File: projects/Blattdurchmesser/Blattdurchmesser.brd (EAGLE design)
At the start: 100 x 80 mm, 14 parts, among them K1 TX2_RELAY", U1 ARDUINOR3-DIMENSION

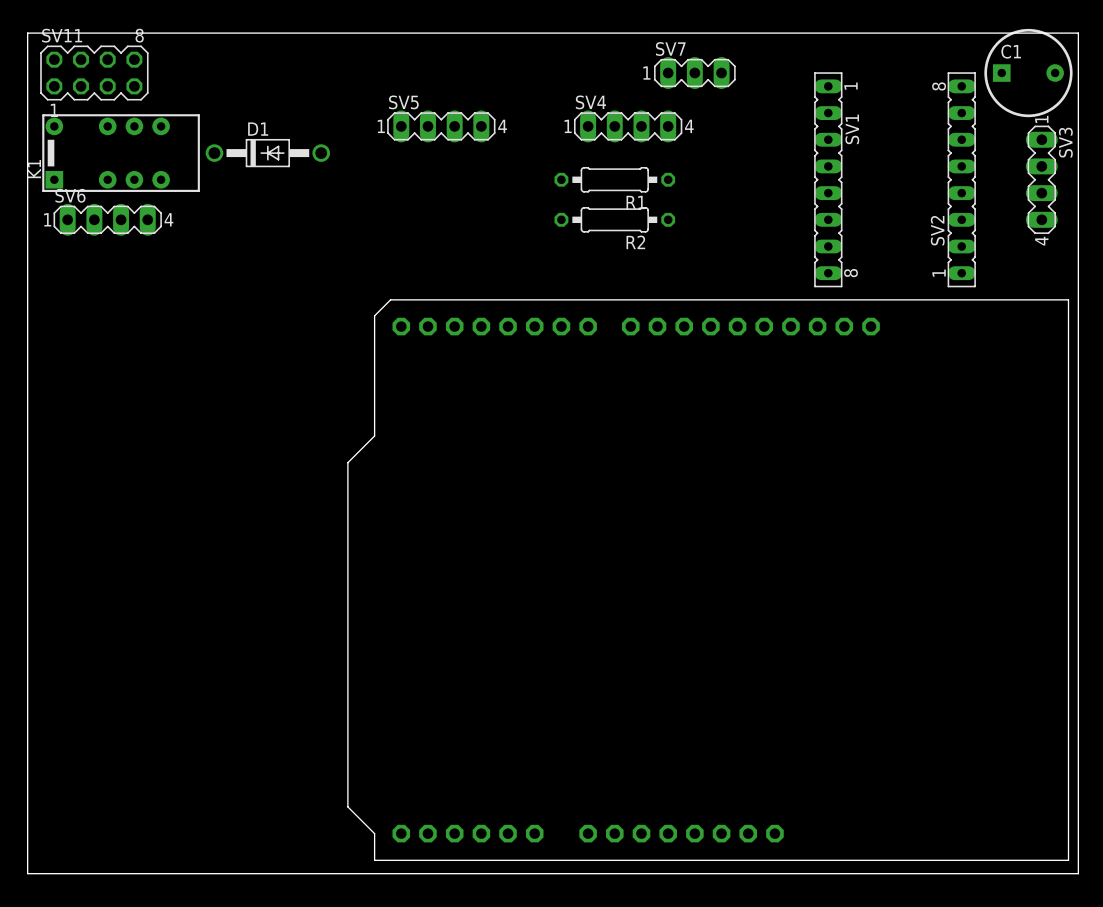
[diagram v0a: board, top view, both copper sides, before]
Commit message: improvement; * parts on pcb rearranged
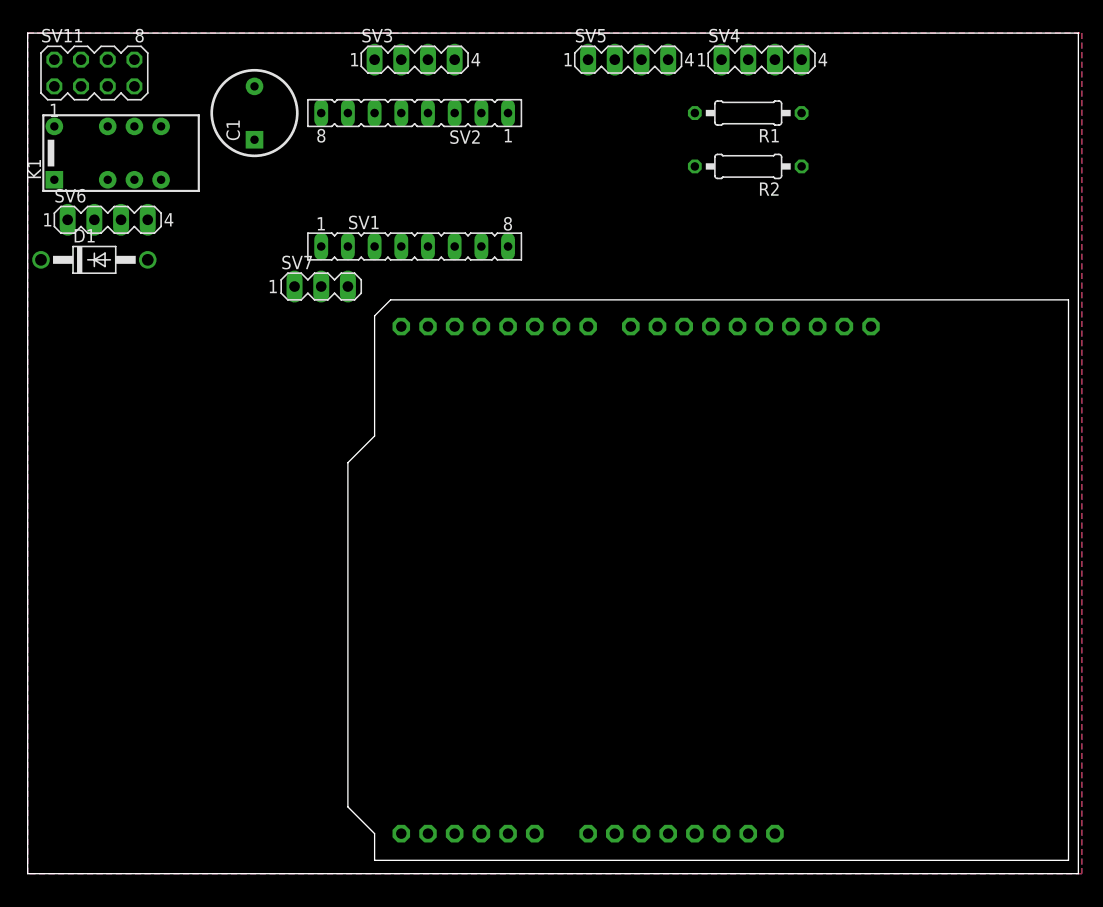
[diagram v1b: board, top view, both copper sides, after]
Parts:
- moved C1 72.6 mm to (21.6, 71.1), turned to 90 degrees
- moved SV3 60.8 mm to (36.8, 77.5), turned to 0 degrees
- moved SV2 52.5 mm to (36.8, 72.4), turned to 180 degrees
- moved SV7 41.0 mm to (27.9, 55.9)
- moved SV1 39.9 mm to (36.8, 59.7), turned to 0 degrees
- moved D1 19.4 mm to (6.35, 58.4)
- moved SV5 18.9 mm to (57.1, 77.5)
- moved R1 14.2 mm to (68.6, 72.4)
- moved SV4 14.2 mm to (69.8, 77.5)
- moved R2 13.7 mm to (68.6, 67.3)
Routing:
- added copper zone on layer 1, net +5V
- added copper zone on layer 16, net GND

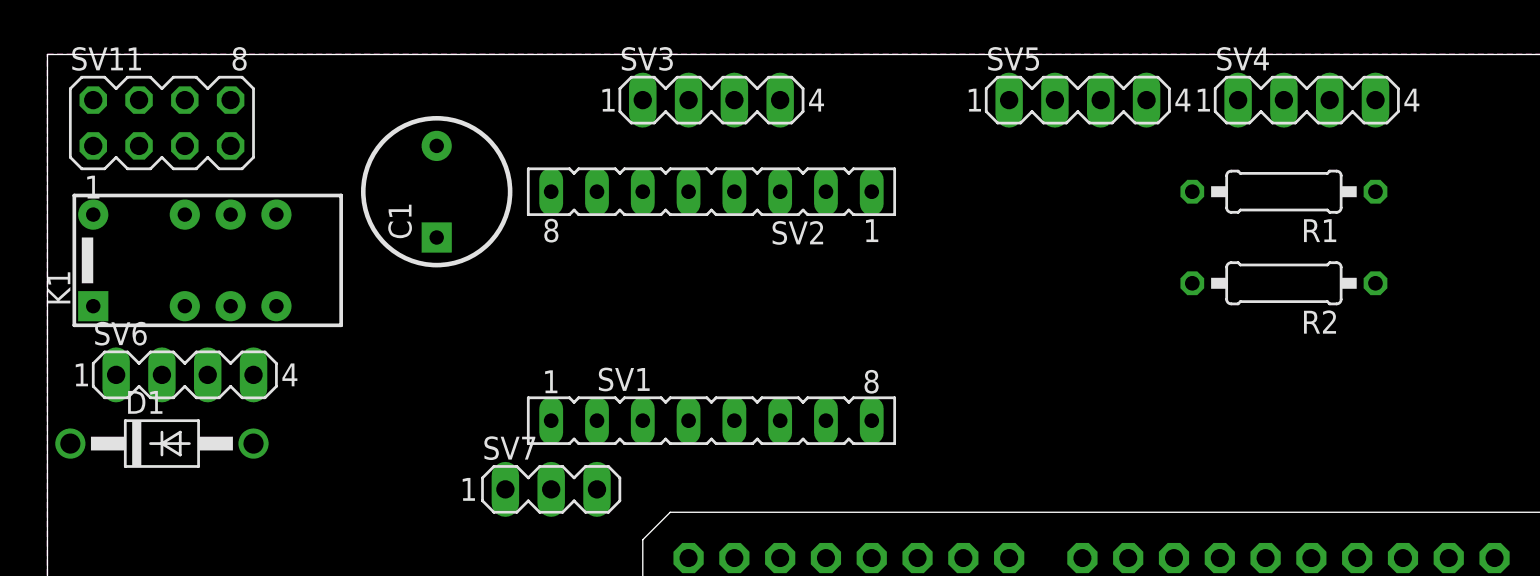
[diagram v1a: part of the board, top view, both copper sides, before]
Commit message: improvement; * fix erdc Dimension Errors
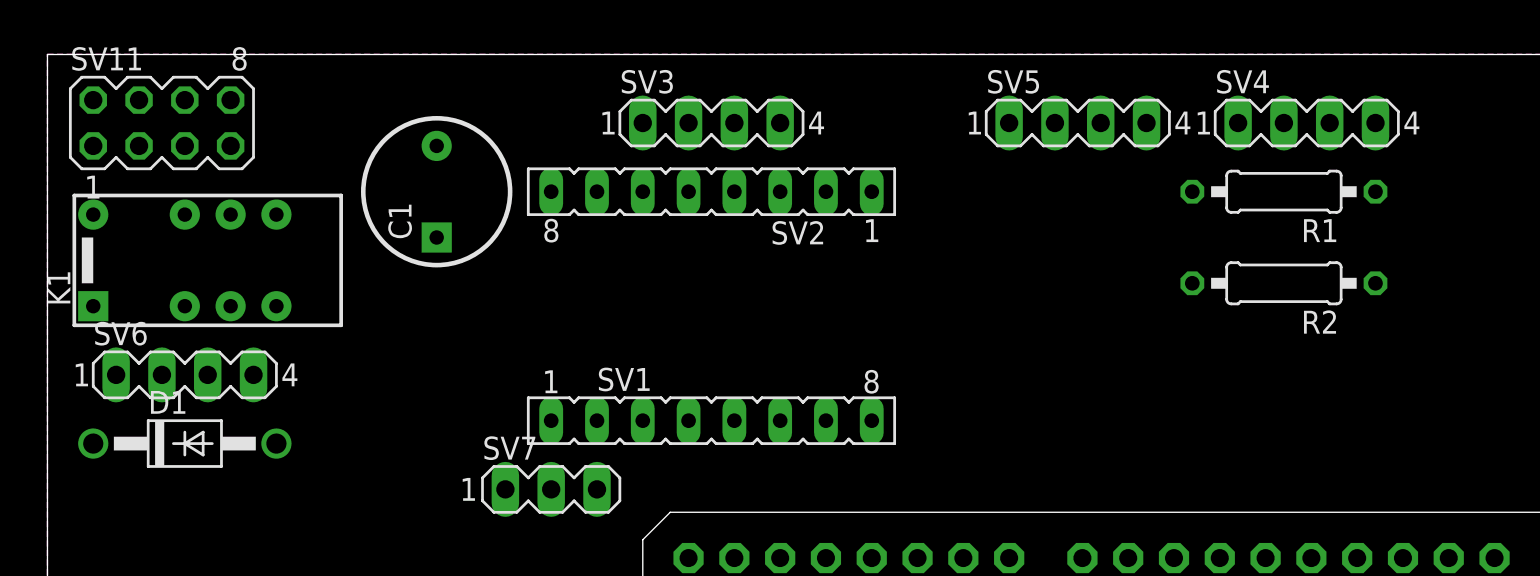
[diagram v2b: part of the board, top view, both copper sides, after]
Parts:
- moved D1 1.27 mm to (7.62, 58.4)
- moved SV3 1.27 mm to (36.8, 76.2)
- moved SV4 1.27 mm to (69.8, 76.2)
- moved SV5 1.27 mm to (57.1, 76.2)
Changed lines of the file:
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@@
 <attribute name="MF" value="" x="36.83" y="72.39" size="1.778" layer="27" rot="R180" display="off"/>
 </element>
-<element name="SV4" library="con-lstb" package="MA04-1" value="" x="69.85" y="77.47">
-<attribute name="MPN" value="" x="69.85" y="77.47" size="1.778" layer="27" display="off"/>
-<attribute name="OC_NEWARK" value="unknown" x="69.85" y="77.47" size="1.778" layer="27" display="off"/>
-<attribute name="OC_FARNELL" value="unknown" x="69.85" y="77.47" size="1.778" layer="27" display="off"/>
-<attribute name="MF" value="" x="69.85" y="77.47" size="1.778" layer="27" display="off"/>
+<element name="SV4" library="con-lstb" package="MA04-1" value="" x="69.85" y="76.2">
+<attribute name="MPN" value="" x="69.85" y="76.2" size="1.778" layer="27" display="off"/>
+<attribute name="OC_NEWARK" value="unknown" x="69.85" y="76.2" size="1.778" layer="27" display="off"/>
+<attribute name="OC_FARNELL" value="unknown" x="69.85" y="76.2" size="1.778" layer="27" display="off"/>
+<attribute name="MF" value="" x="69.85" y="76.2" size="1.778" layer="27" display="off"/>
 </element>
 <element name="SV11" library="con-lstb" package="MA04-2" value="" x="6.35" y="76.2">
@@
 <attribute name="MF" value="" x="6.35" y="76.2" size="1.778" layer="27" display="off"/>
 </element>
-<element name="SV3" library="con-lstb" package="MA04-1" value="" x="36.83" y="77.47">
-<attribute name="MPN" value="" x="36.83" y="77.47" size="1.778" layer="27" display="off"/>
-<attribute name="OC_NEWARK" value="unknown" x="36.83" y="77.47" size="1.778" layer="27" display="off"/>
-<attribute name="OC_FARNELL" value="unknown" x="36.83" y="77.47" size="1.778" layer="27" display="off"/>
-<attribute name="MF" value="" x="36.83" y="77.47" size="1.778" layer="27" display="off"/>
+<element name="SV3" library="con-lstb" package="MA04-1" value="" x="36.83" y="76.2">
+<attribute name="MPN" value="" x="36.83" y="76.2" size="1.778" layer="27" display="off"/>
+<attribute name="OC_NEWARK" value="unknown" x="36.83" y="76.2" size="1.778" layer="27" display="off"/>
+<attribute name="OC_FARNELL" value="unknown" x="36.83" y="76.2" size="1.778" layer="27" display="off"/>
+<attribute name="MF" value="" x="36.83" y="76.2" size="1.778" layer="27" display="off"/>
 </element>
 <element name="C1" library="Elkos" package="R_ELK_8.1" value="R_ELKO_8.1" x="21.59" y="71.12" rot="R90"/>
-<element name="SV5" library="con-lstb" package="MA04-1" value="" x="57.15" y="77.47">
-<attribute name="MPN" value="" x="57.15" y="77.47" size="1.778" layer="27" display="off"/>
-<attribute name="OC_NEWARK" value="unknown" x="57.15" y="77.47" size="1.778" layer="27" display="off"/>
-<attribute name="OC_FARNELL" value="unknown" x="57.15" y="77.47" size="1.778" layer="27" display="off"/>
-<attribute name="MF" value="" x="57.15" y="77.47" size="1.778" layer="27" display="off"/>
+<element name="SV5" library="con-lstb" package="MA04-1" value="" x="57.15" y="76.2">
+<attribute name="MPN" value="" x="57.15" y="76.2" size="1.778" layer="27" display="off"/>
+<attribute name="OC_NEWARK" value="unknown" x="57.15" y="76.2" size="1.778" layer="27" display="off"/>
+<attribute name="OC_FARNELL" value="unknown" x="57.15" y="76.2" size="1.778" layer="27" display="off"/>
+<attribute name="MF" value="" x="57.15" y="76.2" size="1.778" layer="27" display="off"/>
 </element>
 <element name="R1" library="rcl" package="0207/10" value="?" x="68.58" y="72.39" rot="R180"/>
@@
 <attribute name="MF" value="" x="7.62" y="62.23" size="1.778" layer="27" display="off"/>
 </element>
-<element name="D1" library="diode" package="DO41-10" value="1N4004" x="6.35" y="58.42"/>
+<element name="D1" library="diode" package="DO41-10" value="1N4004" x="7.62" y="58.42"/>
 <element name="SV7" library="con-lstb" package="MA03-1" value="" x="27.94" y="55.88">
 <attribute name="MPN" value="" x="27.94" y="55.88" size="1.778" layer="27" display="off"/>
@@
 <vertex x="0" y="0"/>
 </polygon>
-<wire x1="73.66" y1="77.47" x2="72.644" y2="52.07" width="0" layer="19" extent="1-1"/>
+<wire x1="73.66" y1="76.2" x2="72.644" y2="52.07" width="0" layer="19" extent="1-1"/>
 </signal>
 <signal name="VIN">
@@
 <wire x1="21.59" y1="69.85" x2="27.94" y2="72.39" width="0" layer="19" extent="1-1"/>
 <wire x1="2.54" y1="66.04" x2="21.59" y2="69.85" width="0" layer="19" extent="1-1"/>
-<wire x1="1.27" y1="58.42" x2="2.54" y2="66.04" width="0" layer="19" extent="1-1"/>
+<wire x1="2.54" y1="58.42" x2="2.54" y2="66.04" width="0" layer="19" extent="1-1"/>
 </signal>
 <signal name="N$3">
 <contactref element="SV2" pad="6"/>
 <contactref element="SV3" pad="1"/>
-<wire x1="33.02" y1="72.39" x2="33.02" y2="77.47" width="0" layer="19" extent="1-1"/>
+<wire x1="33.02" y1="72.39" x2="33.02" y2="76.2" width="0" layer="19" extent="1-1"/>
 </signal>
 <signal name="N$4">
 <contactref element="SV3" pad="2"/>
 <contactref element="SV2" pad="5"/>
-<wire x1="35.56" y1="72.39" x2="35.56" y2="77.47" width="0" layer="19" extent="1-1"/>
+<wire x1="35.56" y1="72.39" x2="35.56" y2="76.2" width="0" layer="19" extent="1-1"/>
 </signal>
 <signal name="N$5">
 <contactref element="SV2" pad="4"/>
 <contactref element="SV3" pad="3"/>
-<wire x1="38.1" y1="72.39" x2="38.1" y2="77.47" width="0" layer="19" extent="1-1"/>
+<wire x1="38.1" y1="72.39" x2="38.1" y2="76.2" width="0" layer="19" extent="1-1"/>
 </signal>
 <signal name="N$6">
 <contactref element="SV3" pad="4"/>
 <contactref element="SV2" pad="3"/>
-<wire x1="40.64" y1="72.39" x2="40.64" y2="77.47" width="0" layer="19" extent="1-1"/>
+<wire x1="40.64" y1="72.39" x2="40.64" y2="76.2" width="0" layer="19" extent="1-1"/>
 </signal>
 <signal name="N$1">
@@
 <contactref element="R2" pad="1"/>
 <contactref element="U1" pad="D8"/>
-<wire x1="73.66" y1="67.31" x2="71.12" y2="77.47" width="0" layer="19" extent="1-1"/>
+<wire x1="73.66" y1="67.31" x2="71.12" y2="76.2" width="0" layer="19" extent="1-1"/>
 <wire x1="57.404" y1="52.07" x2="73.66" y2="67.31" width="0" layer="19" extent="1-1"/>
 </signal>
@@
 <contactref element="SV5" pad="2"/>
 <contactref element="U1" pad="D10"/>
-<wire x1="62.484" y1="52.07" x2="55.88" y2="77.47" width="0" layer="19" extent="1-1"/>
+<wire x1="62.484" y1="52.07" x2="55.88" y2="76.2" width="0" layer="19" extent="1-1"/>
 </signal>
 <signal name="N$13">
 <contactref element="SV5" pad="4"/>
 <contactref element="U1" pad="D9"/>
-<wire x1="59.944" y1="52.07" x2="60.96" y2="77.47" width="0" layer="19" extent="1-1"/>
+<wire x1="59.944" y1="52.07" x2="60.96" y2="76.2" width="0" layer="19" extent="1-1"/>
 </signal>
 <signal name="N$11">
@@
 <contactref element="D1" pad="A"/>
 <wire x1="6.35" y1="62.23" x2="2.54" y2="71.12" width="0" layer="19" extent="1-1"/>
-<wire x1="11.43" y1="58.42" x2="6.35" y2="62.23" width="0" layer="19" extent="1-1"/>
+<wire x1="12.7" y1="58.42" x2="6.35" y2="62.23" width="0" layer="19" extent="1-1"/>
 </signal>
 <signal name="N$14">
@@
 <contactref element="R1" pad="1"/>
 <contactref element="U1" pad="D2"/>
-<wire x1="73.66" y1="72.39" x2="68.58" y2="77.47" width="0" layer="19" extent="1-1"/>
-<wire x1="40.64" y1="52.07" x2="68.58" y2="77.47" width="0" layer="19" extent="1-1"/>
+<wire x1="73.66" y1="72.39" x2="68.58" y2="76.2" width="0" layer="19" extent="1-1"/>
+<wire x1="40.64" y1="52.07" x2="68.58" y2="76.2" width="0" layer="19" extent="1-1"/>
 </signal>
 </signals>
